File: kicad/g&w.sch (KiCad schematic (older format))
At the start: 191 parts, among them IC1 audio, IC2 MX25U8035FM2, IC3 vreg, IC4 pmic, IC5 BQ24072RGT_, J1 speaker, J2 SWD PORT, J3 DISPLAY1, J4 DISPLAY2, J5 Battery, J6 USB-C, Q1 PMBT3904, Q2 PMBT3904, Q3 PMBT3904, Q4 SSM6J412TU, Y1 H01717

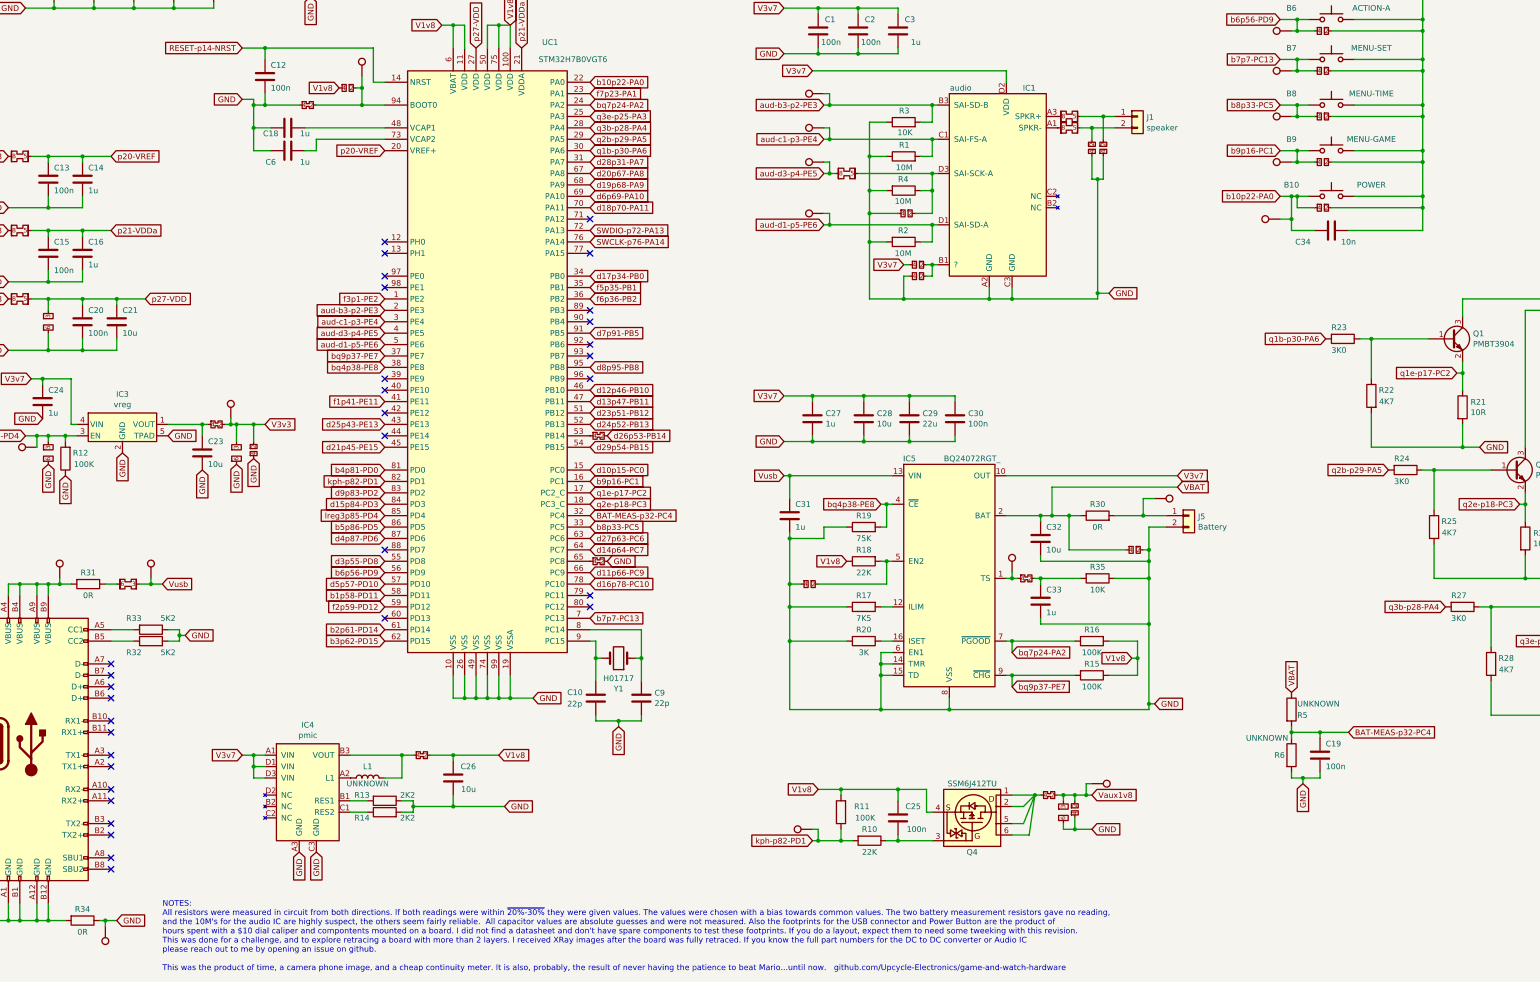
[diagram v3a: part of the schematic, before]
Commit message: Updated Trace&Schematic with new parts numbers. Made new footprints for both BGA's and 3v3 reg. Still need to revise USB-C connector footprint.
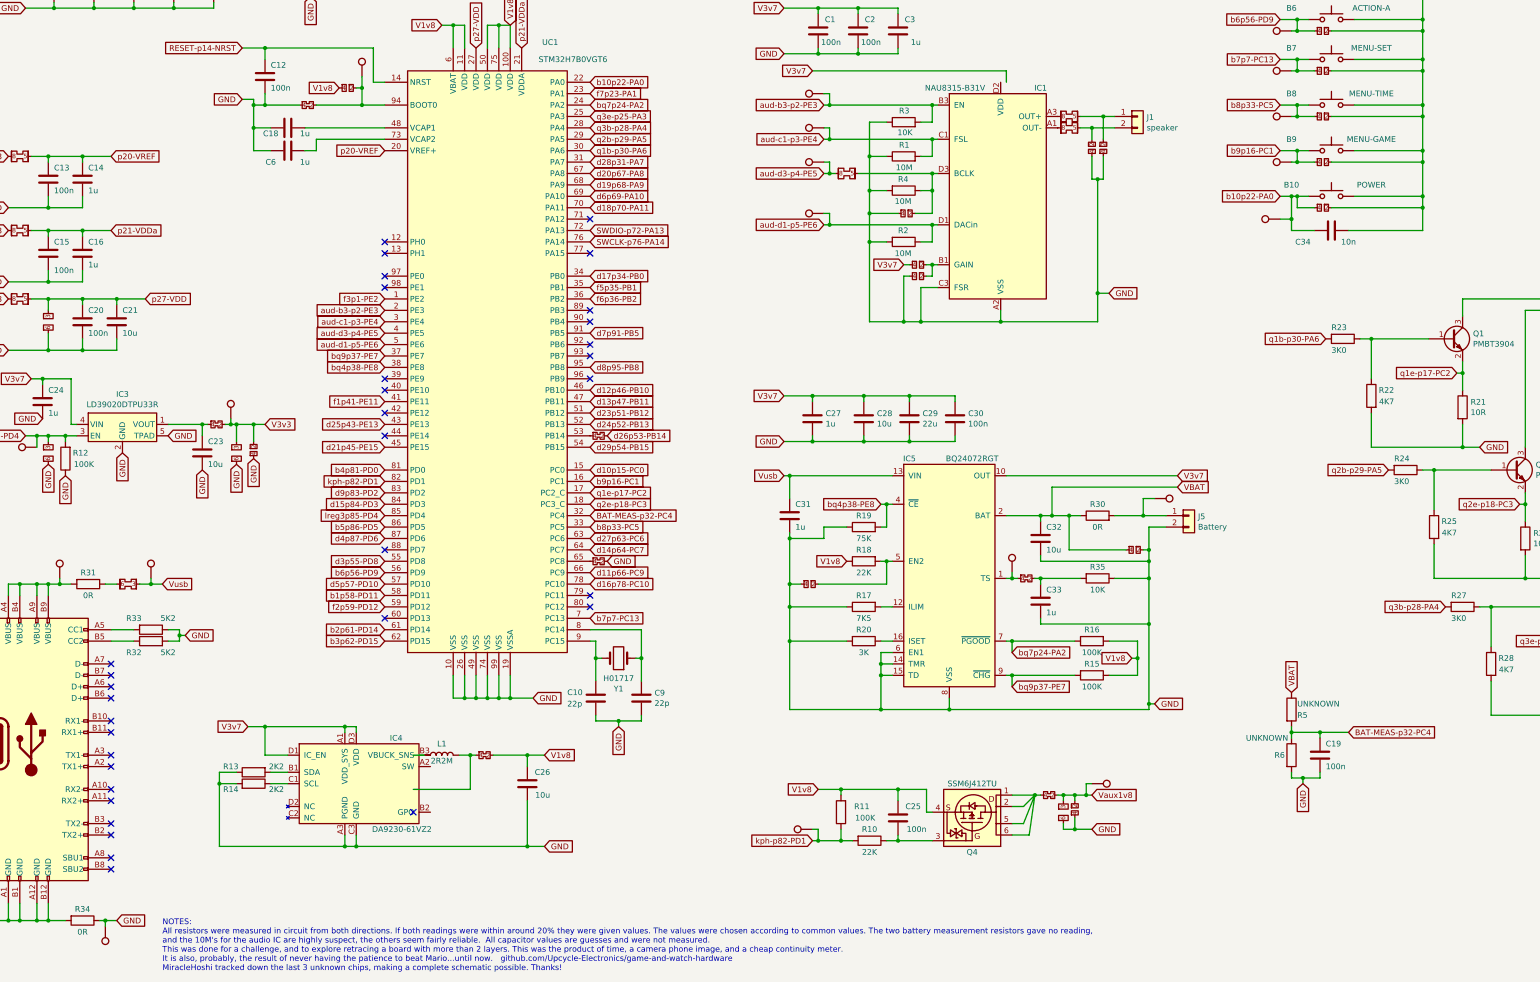
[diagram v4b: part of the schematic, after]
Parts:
- removed IC1: audio, Package_BGA:Texas_DSBGA-12_1.36x1.86mm_Layout3x4_P0.5mm, symbol gnw_library:audio
- removed IC4: pmic, Package_BGA:Texas_DSBGA-12_1.36x1.86mm_Layout3x4_P0.5mm, symbol gnw_library:pmic
- added IC1: NAU8315-B31V, gnw:WLCSP-12_1.18x1.95_Layout3x4_P0.4mm, symbol gnw_library:NAU8315
- added IC4: DA9230-61VZ2, gnw:WLCSP-12_1.28x1.68_Layout3x4_P0.4mm, symbol gnw_library:DA9230-61VZ2
- IC3: value vreg -> LD39020DTPU33R; footprint Package_SON:Texas_X2SON-4_1x1mm_P0.65mm -> gnw:DFN-4-1EP_1x1_P0.65mm_EP0.56x0.56mm
- IC5: value BQ24072RGT_ -> BQ24072RGT
- L1: value UNKNOWN -> 2R2M
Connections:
- net GND: now also IC1.A2 (VSS), IC1.C3 (FSR), IC4.A3 (PGND), IC4.C3 (GND)
- net V3v7: now also IC4.A1 (VDD_SYS), IC4.D1 (IC_EN), IC4.D3 (VDD)
- net aud-b3-p2-PE3: now also IC1.B3 (EN)
- net aud-c1-p3-PE4: now also IC1.C1 (FSL)
- net aud-d1-p5-PE6: now also IC1.D1 (DACin)
- net at R13.2: now also IC4.B1 (SDA)
- net at R14.1: now also IC4.C1 (SCL)
- net at JP84.1: now also IC1.A1 (OUT-)
- net at JP83.1: now also IC1.A3 (OUT+)
- net at JP79.2, JP80.2: now also IC1.B1 (GAIN)
- net at JP77.2, JP78.2, R4.1: now also IC1.D3 (BCLK)
- new net: IC1.B2 (VDD), IC1.C2 (VDD), IC1.D2 (VDD)
- no-connect marks 33 -> 34
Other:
- note added: "NOTES:\nAll resistors were measured in circuit from both directions. If both readings were within around 20% they were given values. The values were chosen according to common values. The two battery measurement resistors gave no reading, \nand the 10M's for the audio IC are highly suspect, the others seem fairly reliable. All capacitor values are guesses and were not measured.\nThis was done for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"
- note removed: "NOTES:\nAll resistors were measured in circuit from both directions. If both readings were within ~20%-30% they were given values. The values were chosen with a bias towards common values. The two battery measurement resistors gave no reading, \nand the 10M's for the audio IC are highly suspect, the others seem fairly reliable. All capacitor values are absolute guesses and were not measured. Also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"
- moved on the sheet: C26, L1, R13, R14

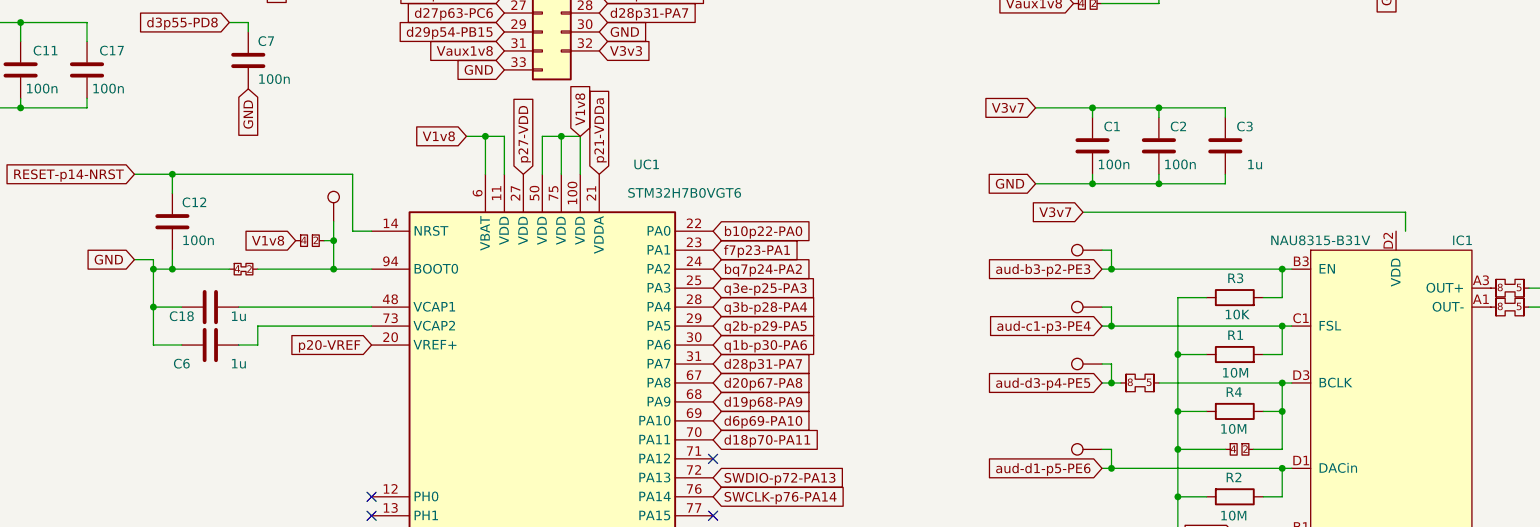
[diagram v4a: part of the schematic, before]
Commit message: USB-C footprint updated from datasheet drawing 1:1 with critical dimensions layer in PCBnew
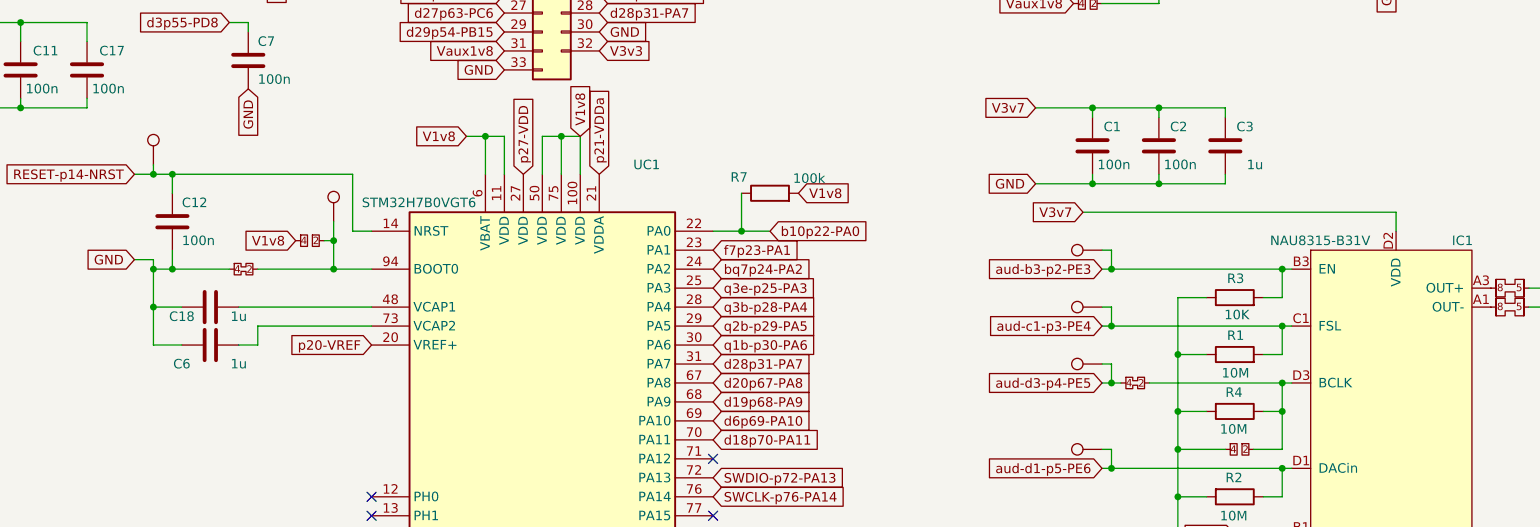
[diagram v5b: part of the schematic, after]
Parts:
- removed JP77: jmp-0805, gnw:JMP-0805-CLOSED, symbol gnw_library:jmp-0805
- added JP77: JMP-0402-CLOSED, gnw:JMP-0402-CLOSED, symbol gnw_library:JMP-0402-CLOSED
- added R7: 100k, Resistor_SMD:R_0201_0603Metric, symbol Device:R
- added TP81: TestPoint, gnw:gnw-TestPoint_Pad_D1.0mm, symbol Connector:TestPoint
- J6: footprint gnw:USB_C_Receptacle_NintendoG&W -> gnw:USB_C_Receptacle_JAE_DX07BN24JA2
- JP100, JP101, JP103, JP104, JP105, JP59, JP60, JP61, JP62, JP63, JP64, JP65, JP66, JP68, JP71, JP74, JP75, JP76, JP78, JP79, JP80, JP81, JP86, JP87, JP90, JP91, JP92, JP93, JP94, JP95, JP96, JP97, JP98, JP99: footprint Resistor_SMD:R_0402_1005Metric_Pad0.72x0.64mm_HandSolder -> Resistor_SMD:R_0402_1005Metric
- JP54, JP55, JP58, JP89: footprint Resistor_SMD:R_0603_1608Metric_Pad0.98x0.95mm_HandSolder -> Resistor_SMD:R_0603_1608Metric
- L1: footprint Inductor_SMD:L_1008_2520Metric_Pad1.43x2.20mm_HandSolder -> Resistor_SMD:R_0402_1005Metric
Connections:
- net RESET-p14-NRST: now also TP81.1
- net V1v8: now also R7.2
- net V3v7: now also IC1.B2 (VDD), IC1.C2 (VDD), IC1.D2 (VDD)
- net aud-d3-p4-PE5: now also JP77.1
- net b10p22-PA0: now also R7.1
- net at IC1.D3 (BCLK), JP78.2, R4.1: now also JP77.2
